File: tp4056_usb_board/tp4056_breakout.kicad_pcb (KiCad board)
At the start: 2 copper layers, 13 parts, among them J2 CONN_02X04, J3 DW01, J4 8205A

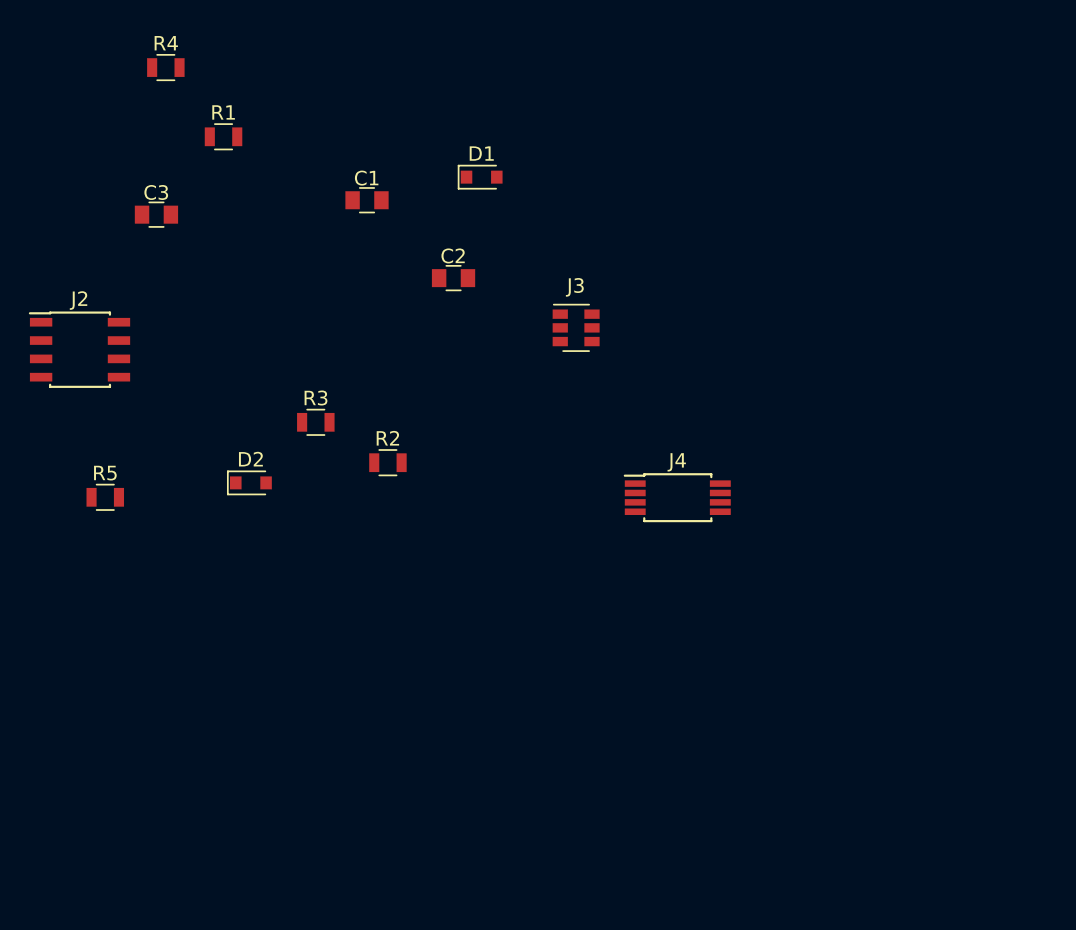
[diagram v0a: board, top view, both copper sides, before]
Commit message: Started the charging+UART breakout
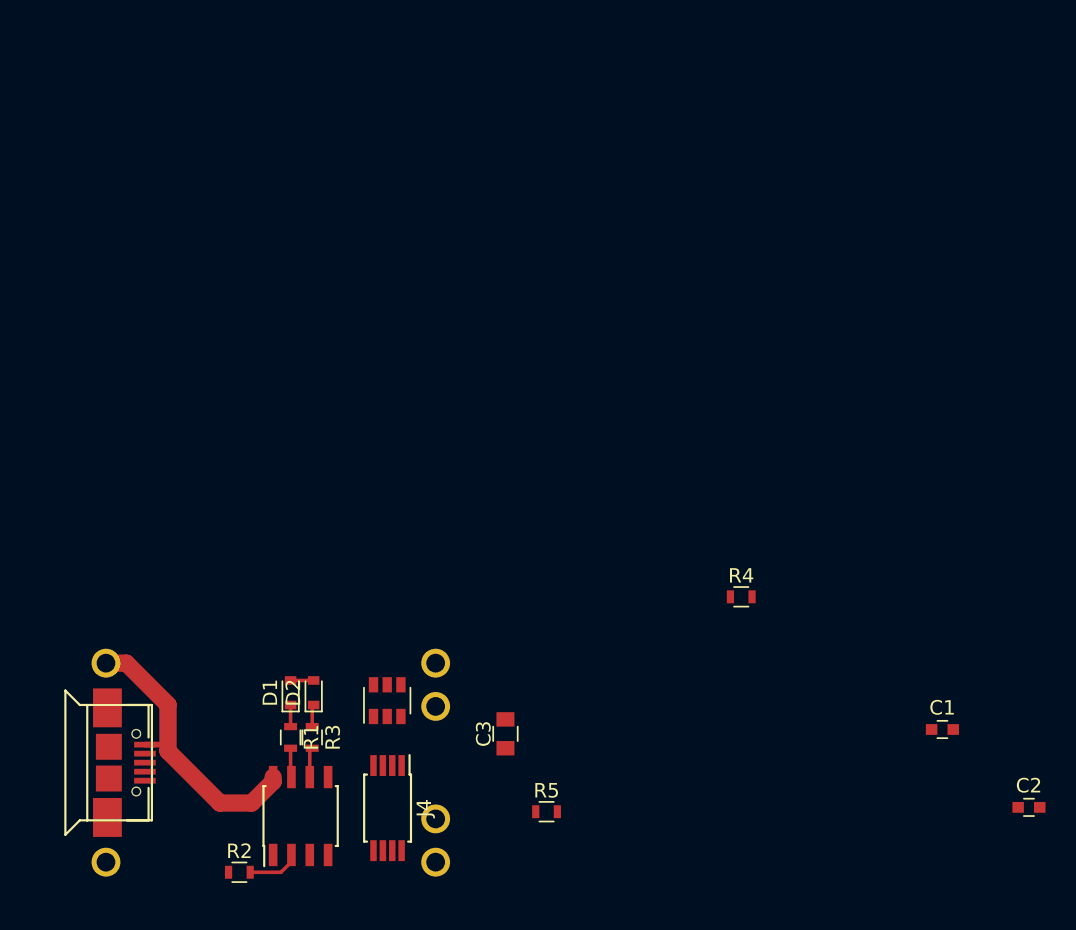
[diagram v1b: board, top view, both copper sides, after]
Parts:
- added J1: USB_OTG, footprints:MICROUSB_SIMPLE, F.Cu at (128.6, 126.0)
- added U1: TP4056_BREAKOUT, tp4056_usb_board:TP4056_BREAKOUT, F.Cu at (137.6, 126.0)
- C1, C2: footprint Capacitors_SMD:C_0805 -> Capacitors_SMD:C_0603
- D1, D2: footprint Diodes_SMD:D_0805 -> Diodes_SMD:D_0603
- R1, R2, R3, R4, R5: footprint Resistors_SMD:R_0805 -> Resistors_SMD:R_0603
- moved C1 54.2 mm to (183.9, 123.7)
- moved C2 54.2 mm to (189.9, 129.1)
- moved R4 54.2 mm to (169.9, 114.5)
- moved C3 43.4 mm to (153.6, 124.0), turned to 90 degrees
- moved R1 41.9 mm to (138.7, 124.2), turned to 270 degrees
- moved D1 38.1 mm to (138.7, 121.2), turned to 90 degrees
- moved R5 37.6 mm to (156.4, 129.4)
- moved J2 35.8 mm to (139.4, 129.7), turned to 90 degrees
- moved R2 30.2 mm to (135.2, 133.6)
- moved J4 29.5 mm to (145.4, 129.2), turned to 270 degrees
- moved J3 29.0 mm to (145.4, 121.7), turned to 90 degrees
- moved R3 21.9 mm to (140.2, 124.2), turned to 270 degrees
- moved D2 15.2 mm to (140.3, 121.2), turned to 90 degrees
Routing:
- net +5V: track 0.00 -> 21.8 mm
- net Net-(J2-Pad2): track 0.00 -> 3.64 mm
- net Net-(J2-Pad6): track 0.00 -> 2.07 mm
- net Net-(J2-Pad7): track 0.00 -> 2.02 mm
- net Net-(D2-Pad1): track 0.00 -> 1.54 mm
- net Net-(D1-Pad1): track 0.00 -> 1.50 mm

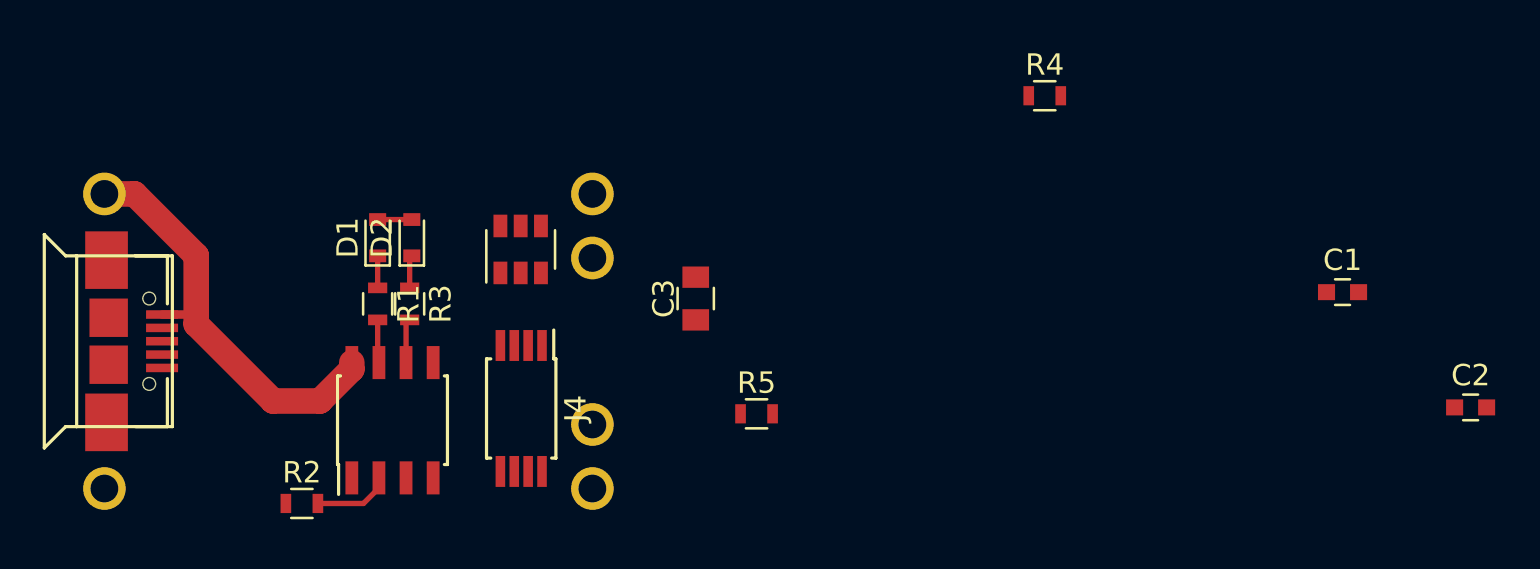
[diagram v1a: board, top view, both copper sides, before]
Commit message: TP4056+UART board almost ready
-Figure out UART castellation placement & add traces to there
-Add thermal vias & mask openings
-Check pads on corners - convert to rectangle pads & enlarge holes
-Verify everything once again against the original boards
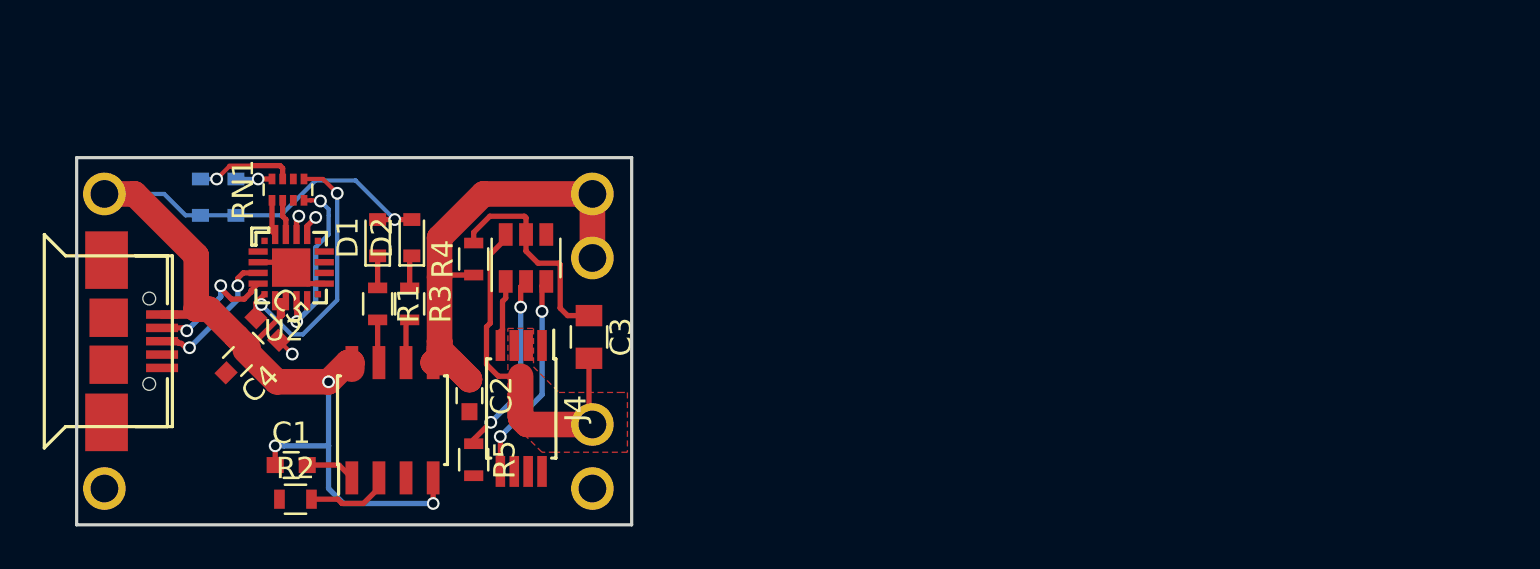
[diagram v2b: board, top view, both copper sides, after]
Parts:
- added C4: 100nF, Capacitors_SMD:C_0603, F.Cu at (132.1, 127.0)
- added C5: 100nF, Capacitors_SMD:C_0603, F.Cu at (133.5, 125.4)
- added D3: LED, Diodes_SMD:D_0603, B.Cu at (130.4, 119.2)
- added D4: LED, Diodes_SMD:D_0603, B.Cu at (132.1, 119.2)
- added RN1: R_Pack04, Resistors_SMD:R_Array_Concave_4x0402, F.Cu at (134.5, 118.9)
- added U2: CP2102N-20P, CP2102N_QFN20:QFN-20-1EP_3x3mm_Pitch0.5, F.Cu at (134.7, 122.5)
- J2: value CONN_02X04 -> TP4056
- moved C1 49.9 mm to (134.7, 131.8)
- moved C2 46.9 mm to (143.0, 128.6), turned to 270 degrees
- moved R4 27.8 mm to (143.2, 122.2), turned to 90 degrees
- moved R5 13.4 mm to (143.2, 131.6), turned to 270 degrees
- moved C3 5.31 mm to (148.6, 125.8), turned to 270 degrees
- moved J3 0.47 mm to (145.7, 122.1)
- moved R2 0.36 mm to (134.8, 133.4)
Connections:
- J1 pad 2: (no net) -> Net-(J1-Pad2)
- J1 pad 3: (no net) -> Net-(J1-Pad3)
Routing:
- net +5V: track 21.8 -> 57.0 mm, vias 0 -> 4
- net VSS: track 0.00 -> 23.0 mm
- net BAT-: track 0.00 -> 16.9 mm
- net VDD: track 0.00 -> 13.2 mm, vias 0 -> 2
- net Net-(C3-Pad1): track 0.00 -> 10.2 mm
- net Net-(J3-Pad3): track 0.00 -> 9.80 mm, vias 0 -> 2
- net Net-(J3-Pad2): track 0.00 -> 8.61 mm, vias 0 -> 2
- net RST: track 0.00 -> 8.20 mm, vias 0 -> 2
- net Net-(J1-Pad3): track 0.00 -> 6.66 mm, vias 0 -> 2
- net Net-(J1-Pad2): track 0.00 -> 6.41 mm, vias 0 -> 2
- net Net-(D3-Pad1): track 0.00 -> 4.66 mm, vias 0 -> 1
- net GND: track 0.00 -> 4.42 mm, vias 0 -> 1
- net Net-(J3-Pad1): track 0.00 -> 3.10 mm
- net Net-(C1-Pad2): track 0.00 -> 2.67 mm
- net (no net): track 0.00 -> 1.87 mm, vias 0 -> 2
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- added copper zone on F.Cu, net BAT-
- added copper zone on B.Cu, net GND
- added copper zone on F.Cu, net GND
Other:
- board outline added: 26 x 17.2 mm

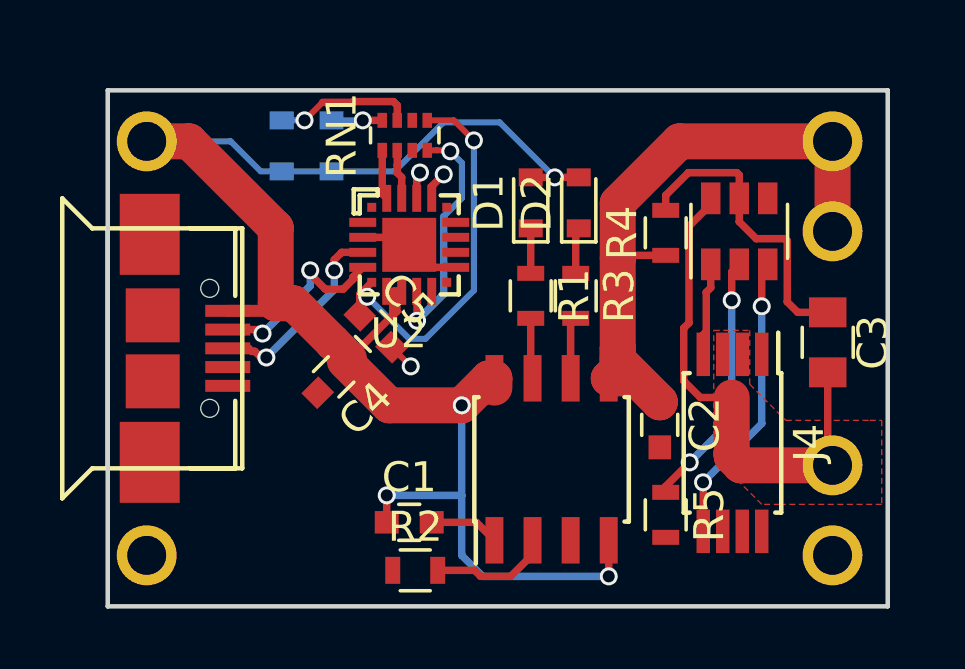
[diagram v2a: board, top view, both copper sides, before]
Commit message: Finished TP4056 charging+USB-UART board
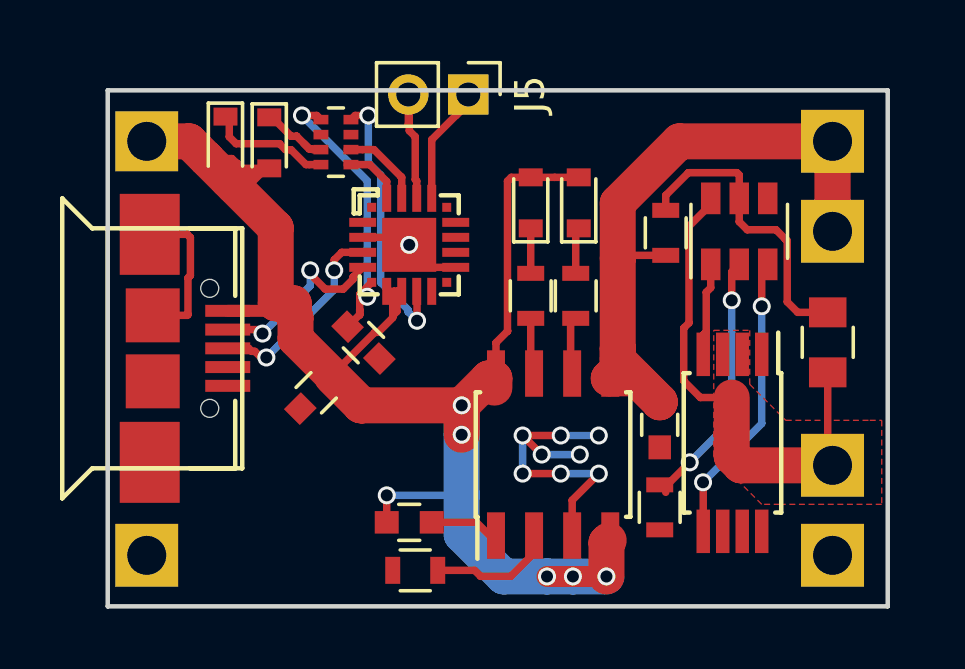
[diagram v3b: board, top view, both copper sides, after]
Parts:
- added J5: TEST_2P, Pin_Headers:Pin_Header_Straight_1x02_Pitch2.00mm, F.Cu at (136.6, 117.5)
- D3, D4: moved to F.Cu
- moved D4 3.54 mm to (128.5, 119.1)
- moved RN1 2.30 mm to (132.2, 119.1), turned to 180 degrees
- moved C4 0.79 mm to (131.5, 127.5)
- moved C5 0.56 mm to (133.1, 125.8)
- moved D3 0.43 mm to (130.0, 119.2)
- moved R5 0.32 mm to (143.0, 131.3)
- moved J2 0.17 mm to (139.4, 129.5)
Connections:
- U2 pad 17: (no net) -> RXD
- U2 pad 18: (no net) -> TXD
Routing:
- net GND: track 4.42 -> 19.7 mm, vias 1 -> 9
- net RXD: track 0.00 -> 5.00 mm
- net TXD: track 0.00 -> 4.34 mm
- net +5V: track 57.0 -> 60.7 mm, vias 4 -> 6
- net VDD: track 13.2 -> 9.89 mm
- net VSS: track 23.0 -> 26.0 mm
- net Net-(D3-Pad1): track 4.66 -> 2.45 mm, vias 1 -> 0
- net Net-(D4-Pad1): track 1.70 -> 3.86 mm, vias 1 -> 0
- net (no net): track 1.87 -> 0.00 mm, vias 2 -> 0
- net RX_LED: track 1.66 -> 2.90 mm
- net RST: track 8.20 -> 9.14 mm
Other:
- board text added: "BAT+"
- board text added: "BAT-"
- board text added: "IN+"
- board text added: "IN-"
- board text added: "LiIon charging + UART board for ZeroPhone v1.0 by CRImier"
- board text added: "OUT+"
- board text added: "OUT-"

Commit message: Added text with LED color-to-signal info
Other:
- board text added: "Red=charging Blue=charged Yellow=TX Green=RX"
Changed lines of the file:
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@@
     (links 58)
     (no_connects 0)
-    (area 122.625 114.29088 151.175 136.727)
+    (area 124.524999 117.324999 150.675001 134.675001)
     (thickness 1.6)
-    (drawings 11)
+    (drawings 12)
     (tracks 278)
     (zones 0)
@@
     )
   )
+  (gr_text "Red=charging\nBlue=charged\nYellow=TX Green=RX" (at 140.97 120.396) (layer B.SilkS)
+    (effects (font (size 0.8 0.8) (thickness 0.2)) (justify left mirror))
+  )
   (gr_text IN+ (at 129.2352 119.1768) (layer B.SilkS)
     (effects (font (size 1.5 1.5) (thickness 0.3)) (justify mirror))
@@
     (effects (font (size 1.5 1.5) (thickness 0.3)) (justify mirror))
   )
-  (gr_text OUT- (at 144.526 132.842) (layer B.SilkS)
+  (gr_text OUT- (at 144.272 132.842) (layer B.SilkS)
     (effects (font (size 1.5 1.5) (thickness 0.3)) (justify mirror))
   )
-  (gr_text BAT- (at 144.6276 129.9464) (layer B.SilkS)
+  (gr_text BAT- (at 144.272 130.048) (layer B.SilkS)
     (effects (font (size 1.5 1.5) (thickness 0.3)) (justify mirror))
   )
@@
     (effects (font (size 1.5 1.5) (thickness 0.3)) (justify mirror))
   )
-  (gr_text "LiIon charging + UART board\nfor ZeroPhone\nv1.0\nby CRImier" (at 136.2964 127.762) (layer B.SilkS)
+  (gr_text "LiIon charging + UART board\nfor ZeroPhone\nv1.0\nby CRImier" (at 136.2964 128.27) (layer B.SilkS)
     (effects (font (size 1 1) (thickness 0.25)) (justify mirror))
   )

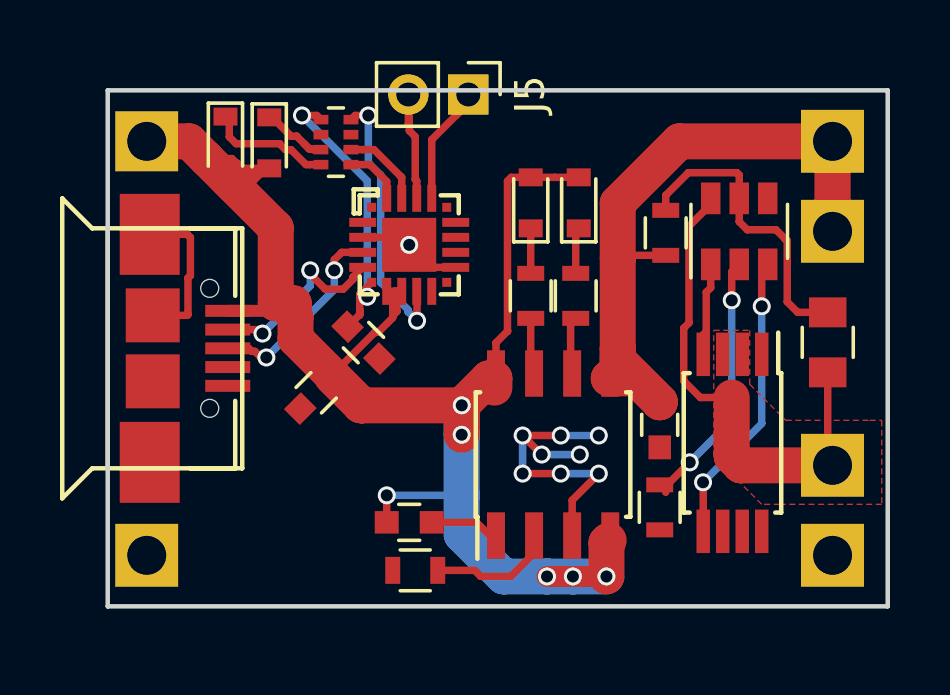
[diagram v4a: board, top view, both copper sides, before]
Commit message: Changed layout/UART header for the new back board
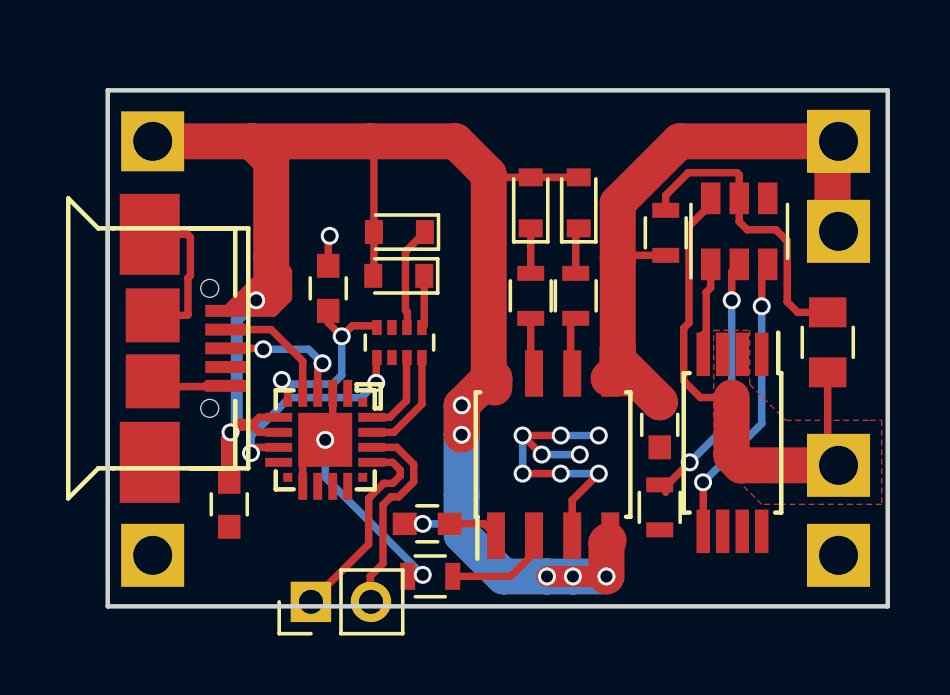
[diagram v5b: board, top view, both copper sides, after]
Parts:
- moved J5 17.7 mm to (131.4, 134.4), turned to 90 degrees
- moved U2 7.08 mm to (131.8, 129.1), turned to 270 degrees
- moved RN1 7.01 mm to (134.3, 125.8), turned to 90 degrees
- moved D4 6.53 mm to (134.3, 122.1), turned to 180 degrees
- moved D3 6.19 mm to (134.3, 123.6), turned to 180 degrees
- moved C4 4.72 mm to (128.7, 131.2), turned to 270 degrees
- moved C5 2.16 mm to (131.9, 124.0), turned to 90 degrees
- moved C1 0.60 mm to (135.2, 131.8)
- moved R2 0.54 mm to (135.3, 133.6)
- moved U1 0.20 mm to (137.8, 126.0)
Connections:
- RN1 pad 1: TX_LED -> RST
- RN1 pad 2: RX_LED -> (no net)
- RN1 pad 3: (no net) -> TX_LED
- RN1 pad 4: RST -> RX_LED
- RN1 pad 5: VDD -> Net-(D3-Pad1)
- RN1 pad 6: (no net) -> Net-(D4-Pad1)
- RN1 pad 7: Net-(D3-Pad1) -> (no net)
- RN1 pad 8: Net-(D4-Pad1) -> VDD
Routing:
- net GND: track 19.7 -> 29.6 mm, vias 9 -> 11
- net +5V: track 60.7 -> 69.4 mm, vias 6 -> 8
- net VDD: track 9.89 -> 6.68 mm
- net TXD: track 4.34 -> 7.12 mm
- net Net-(J1-Pad2): track 6.41 -> 4.01 mm, vias 2 -> 0
- net Net-(J1-Pad3): track 6.66 -> 4.43 mm
- net RXD: track 5.00 -> 6.86 mm
- net RST: track 9.14 -> 7.33 mm
- net TX_LED: track 2.11 -> 2.83 mm
- net RX_LED: track 2.90 -> 3.62 mm
- net Net-(C1-Pad2): track 2.67 -> 2.04 mm
- net Net-(D3-Pad1): track 2.45 -> 1.85 mm
- net Net-(J2-Pad2): track 4.02 -> 3.44 mm
